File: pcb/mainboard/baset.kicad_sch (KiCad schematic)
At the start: 61 parts, among them J27 0826-1G1T-23-F, U33 ECS-1612MV-250-CN, U34 KSZ9031RN, U35 RCLAMP0514M, U36 RCLAMP0514M, U8 XC7K70T-2FBG484C

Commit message: Initial MCU subsystem layout
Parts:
- added C238: 0.47 uF, azonenberg_pcb:EIA_0402_CAP_NOSILK, symbol device:C
- added TP32: U.FL, azonenberg_pcb:CONN_U.FL_TE_1909763-1, symbol conn:CONN_COAXIAL
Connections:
- net 3V3: now also C238.1
- net D1V2: now also TP32.1 (In)
- net GND: now also C238.2, TP32.2 (Ext)
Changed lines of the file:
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@@
   (junction (at 107.95 198.12) (diameter 0) (color 0 0 0 0)
   )
+  (junction (at 68.58 130.81) (diameter 0) (color 0 0 0 0)
+  )
+  (junction (at 68.58 123.19) (diameter 0) (color 0 0 0 0)
+  )
   (junction (at 99.06 78.74) (diameter 0) (color 0 0 0 0)
   )
@@
   (junction (at 223.52 43.18) (diameter 0) (color 0 0 0 0)
   )
+  (junction (at 80.01 160.02) (diameter 0) (color 0 0 0 0)
+  )
   (junction (at 99.06 29.21) (diameter 0) (color 0 0 0 0)
   )
@@
   )
   (junction (at 57.15 265.43) (diameter 0) (color 0 0 0 0)
+  )
+  (junction (at 80.01 152.4) (diameter 0) (color 0 0 0 0)
   )
   (junction (at 86.36 139.7) (diameter 0) (color 0 0 0 0)
@@
     (stroke (width 0) (type default) (color 0 0 0 0))
   )
+  (wire (pts (xy 85.09 130.81) (xy 85.09 128.27))
+    (stroke (width 0) (type default) (color 0 0 0 0))
+  )
   (wire (pts (xy 66.04 152.4) (xy 80.01 152.4))
     (stroke (width 0) (type default) (color 0 0 0 0))
@@
     (stroke (width 0) (type default) (color 0 0 0 0))
   )
+  (wire (pts (xy 68.58 123.19) (xy 81.28 123.19))
+    (stroke (width 0) (type default) (color 0 0 0 0))
+  )
   (wire (pts (xy 58.42 168.91) (xy 53.34 168.91))
     (stroke (width 0) (type default) (color 0 0 0 0))
@@
     (stroke (width 0) (type default) (color 0 0 0 0))
   )
+  (wire (pts (xy 80.01 160.02) (xy 93.98 160.02))
+    (stroke (width 0) (type default) (color 0 0 0 0))
+  )
   (wire (pts (xy 99.06 29.21) (xy 99.06 31.75))
     (stroke (width 0) (type default) (color 0 0 0 0))
@@
     (stroke (width 0) (type default) (color 0 0 0 0))
   )
+  (wire (pts (xy 80.01 152.4) (xy 93.98 152.4))
+    (stroke (width 0) (type default) (color 0 0 0 0))
+  )
   (wire (pts (xy 54.61 66.04) (xy 46.99 66.04))
     (stroke (width 0) (type default) (color 0 0 0 0))
@@
   )
   (wire (pts (xy 72.39 185.42) (xy 68.58 185.42))
+    (stroke (width 0) (type default) (color 0 0 0 0))
+  )
+  (wire (pts (xy 68.58 130.81) (xy 85.09 130.81))
     (stroke (width 0) (type default) (color 0 0 0 0))
   )
@@
     )
     (property "Datasheet" "" (id 3) (at 58.42 96.52 0)
+      (effects (font (size 1.27 1.27)) hide)
+    )
+    (pin "1")
+    (pin "2")
+  )
+  (symbol (lib_id "conn:CONN_COAXIAL") (at 85.09 123.19 0) (unit 1)
+    (in_bom yes) (on_board yes) (fields_autoplaced)
+    (property "Reference" "TP32" (id 0) (at 87.6301 122.6485 0)
+      (effects (font (size 1.27 1.27)) (justify left))
+    )
+    (property "Value" "U.FL" (id 1) (at 87.6301 125.1854 0)
+      (effects (font (size 1.27 1.27)) (justify left))
+    )
+    (property "Footprint" "azonenberg_pcb:CONN_U.FL_TE_1909763-1" (id 2) (at 85.09 123.19 0)
+      (effects (font (size 1.27 1.27)) hide)
+    )
+    (property "Datasheet" "" (id 3) (at 85.09 123.19 0)
       (effects (font (size 1.27 1.27)) hide)
     )
@@
       (effects (font (size 1.27 1.27)) hide)
     )
+    (pin "1")
+    (pin "2")
+  )
+  (symbol (lib_id "device:C") (at 93.98 156.21 0) (unit 1)
+    (in_bom yes) (on_board yes)
+    (property "Reference" "C238" (id 0) (at 96.901 155.0416 0)
+      (effects (font (size 1.27 1.27)) (justify left))
+    )
+    (property "Value" "0.47 uF" (id 1) (at 96.901 157.353 0)
+      (effects (font (size 1.27 1.27)) (justify left))
+    )
+    (property "Footprint" "azonenberg_pcb:EIA_0402_CAP_NOSILK" (id 2) (at 94.9452 160.02 0)
+      (effects (font (size 1.27 1.27)) hide)
+    )
+    (property "Datasheet" "" (id 3) (at 93.98 156.21 0)
+      (effects (font (size 1.27 1.27)) hide)
+    )

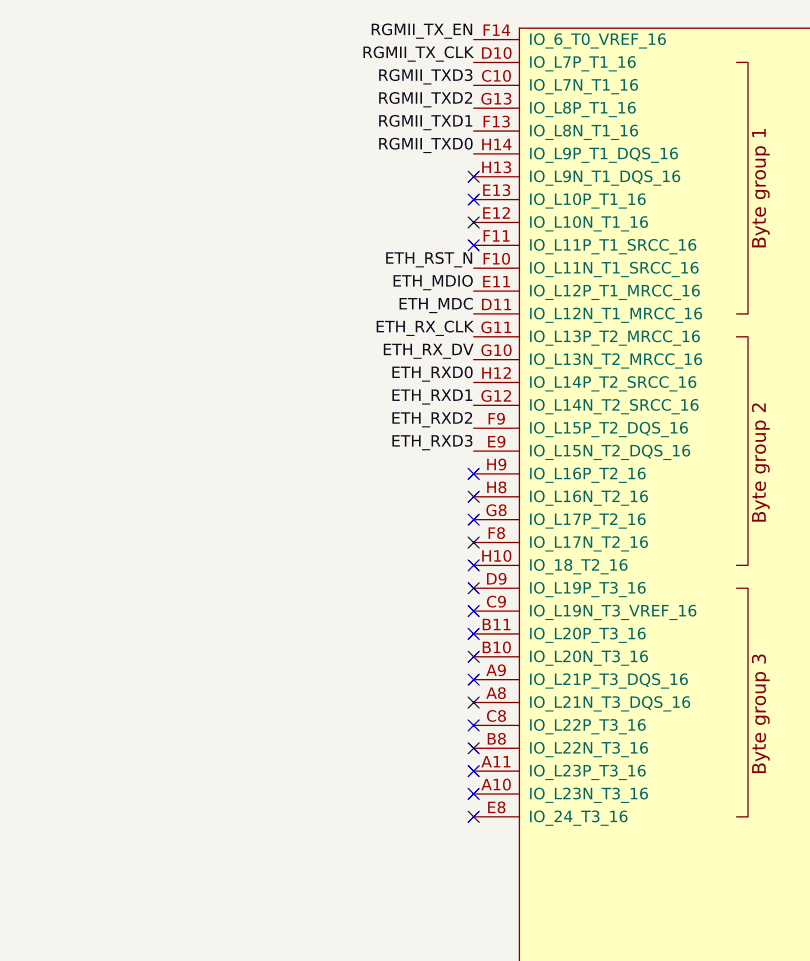
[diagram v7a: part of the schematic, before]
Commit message: Initial FPGA routing
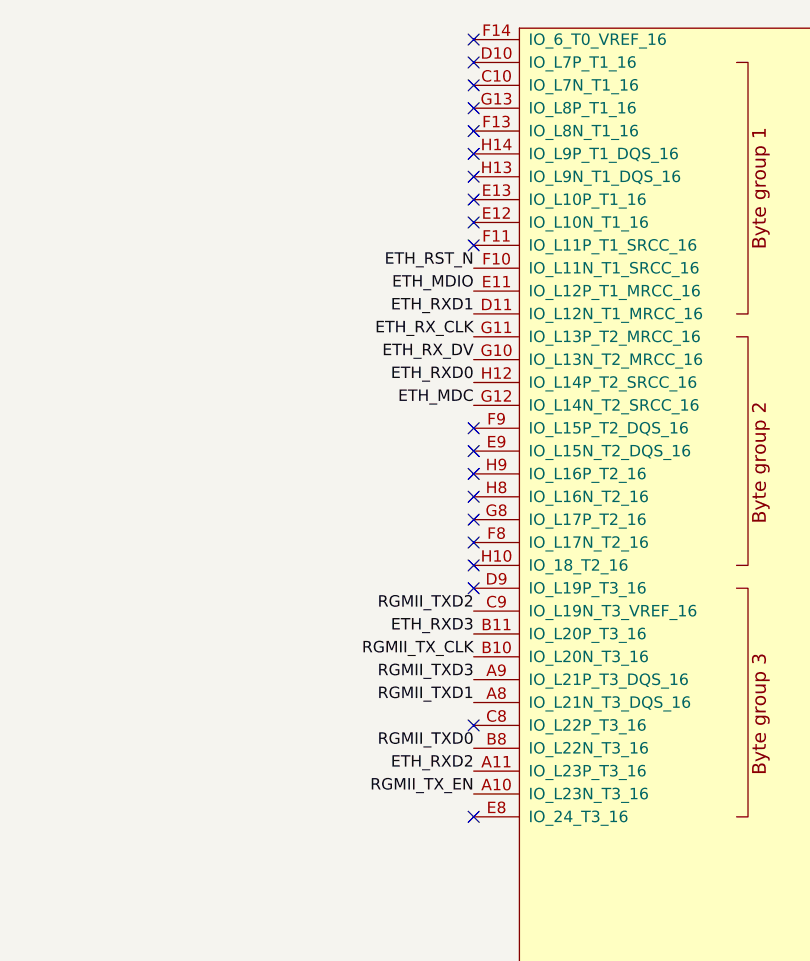
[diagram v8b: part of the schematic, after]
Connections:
- net ETH_MDC: now also U8.G12 (IO_L14N_T2_SRCC_16); no longer U8.D11 (IO_L12N_T1_MRCC_16)
- net ETH_RXD1: now also U8.D11 (IO_L12N_T1_MRCC_16); no longer U8.G12 (IO_L14N_T2_SRCC_16)
- net ETH_RXD2: now also U8.A11 (IO_L23P_T3_16); no longer U8.F9 (IO_L15P_T2_DQS_16)
- net ETH_RXD3: now also U8.B11 (IO_L20P_T3_16); no longer U8.E9 (IO_L15N_T2_DQS_16)
- net RGMII_TXD0: now also U8.B8 (IO_L22N_T3_16); no longer U8.H14 (IO_L9P_T1_DQS_16)
- net RGMII_TXD1: now also U8.A8 (IO_L21N_T3_DQS_16); no longer U8.F13 (IO_L8N_T1_16)
- net RGMII_TXD2: now also U8.C9 (IO_L19N_T3_VREF_16); no longer U8.G13 (IO_L8P_T1_16)
- net RGMII_TXD3: now also U8.A9 (IO_L21P_T3_DQS_16); no longer U8.C10 (IO_L7N_T1_16)
- net RGMII_TX_CLK: now also U8.B10 (IO_L20N_T3_16); no longer U8.D10 (IO_L7P_T1_16)
- net RGMII_TX_EN: now also U8.A10 (IO_L23N_T3_16); no longer U8.F14 (IO_6_T0_VREF_16)
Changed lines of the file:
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@@
   (title_block
     (title "Trigger Crossbar")
-    (date "2023-12-20")
+    (date "2023-12-22")
     (rev "0.1")
     (company "Antikernel Labs")
@@
   (junction (at 85.09 185.42) (diameter 0) (color 0 0 0 0)
   )
+  (no_connect (at 347.98 66.04))
+  (no_connect (at 347.98 20.32))
   (no_connect (at 99.06 71.12))
-  (no_connect (at 347.98 99.06))
+  (no_connect (at 347.98 25.4))
   (no_connect (at 347.98 40.64))
-  (no_connect (at 347.98 86.36))
   (no_connect (at 347.98 71.12))
   (no_connect (at 347.98 35.56))
   (no_connect (at 347.98 38.1))
-  (no_connect (at 347.98 83.82))
-  (no_connect (at 347.98 104.14))
+  (no_connect (at 347.98 33.02))
   (no_connect (at 347.98 81.28))
   (no_connect (at 347.98 76.2))
   (no_connect (at 347.98 78.74))
-  (no_connect (at 347.98 88.9))
-  (no_connect (at 347.98 93.98))
-  (no_connect (at 347.98 101.6))
+  (no_connect (at 347.98 27.94))
+  (no_connect (at 347.98 30.48))
   (no_connect (at 156.21 90.17))
   (no_connect (at 347.98 96.52))
@@
   (no_connect (at 347.98 68.58))
   (no_connect (at 347.98 43.18))
-  (no_connect (at 347.98 91.44))
+  (no_connect (at 347.98 22.86))
+  (no_connect (at 347.98 63.5))
   (wire (pts (xy 223.52 45.72) (xy 223.52 43.18))
     (stroke (width 0) (type default) (color 0 0 0 0))
@@
     (effects (font (size 1.27 1.27)) (justify left bottom))
   )
-  (label "RGMII_TXD3" (at 347.98 25.4 180)
+  (label "RGMII_TXD3" (at 347.98 91.44 180)
     (effects (font (size 1.27 1.27)) (justify right bottom))
   )
@@
     (effects (font (size 1.27 1.27)) (justify left bottom))
   )
-  (label "RGMII_TX_EN" (at 347.98 20.32 180)
+  (label "RGMII_TX_EN" (at 347.98 104.14 180)
     (effects (font (size 1.27 1.27)) (justify right bottom))
   )
@@
     (effects (font (size 1.27 1.27)) (justify right bottom))
   )
-  (label "RGMII_TXD1" (at 347.98 30.48 180)
+  (label "RGMII_TXD1" (at 347.98 93.98 180)
     (effects (font (size 1.27 1.27)) (justify right bottom))
   )
@@
     (effects (font (size 1.27 1.27)) (justify left bottom))
   )
-  (label "ETH_RXD1" (at 347.98 60.96 180)
+  (label "ETH_RXD1" (at 347.98 50.8 180)
     (effects (font (size 1.27 1.27)) (justify right bottom))
   )
@@
     (effects (font (size 1.27 1.27)) (justify right bottom))
   )
-  (label "RGMII_TX_CLK" (at 347.98 22.86 180)
-    (effects (font (size 1.27 1.27)) (justify right bottom))
-  )
-  (label "ETH_RXD2" (at 347.98 63.5 180)
+  (label "RGMII_TX_CLK" (at 347.98 88.9 180)
+    (effects (font (size 1.27 1.27)) (justify right bottom))
+  )
+  (label "ETH_RXD2" (at 347.98 101.6 180)
     (effects (font (size 1.27 1.27)) (justify right bottom))
   )
@@
     (effects (font (size 1.27 1.27)) (justify right bottom))
   )
-  (label "ETH_RXD3" (at 347.98 66.04 180)
-    (effects (font (size 1.27 1.27)) (justify right bottom))
-  )
-  (label "ETH_MDC" (at 347.98 50.8 180)
+  (label "ETH_RXD3" (at 347.98 86.36 180)
+    (effects (font (size 1.27 1.27)) (justify right bottom))
+  )
+  (label "ETH_MDC" (at 347.98 60.96 180)
     (effects (font (size 1.27 1.27)) (justify right bottom))
   )
@@
     (effects (font (size 1.27 1.27)) (justify right bottom))
   )
-  (label "RGMII_TXD2" (at 347.98 27.94 180)
+  (label "RGMII_TXD2" (at 347.98 83.82 180)
     (effects (font (size 1.27 1.27)) (justify right bottom))
   )
@@
     (effects (font (size 1.27 1.27)) (justify right bottom))
   )
-  (label "RGMII_TXD0" (at 347.98 33.02 180)
-    (effects (font (size 1.27 1.27)) (justify right bottom))
-  )
+  (label "RGMII_TXD0" (at 347.98 99.06 180)
+    (effects (font (size 1.27 1.27)) (justify right bottom))
+  )
